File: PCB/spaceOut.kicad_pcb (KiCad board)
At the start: 2 copper layers, 98.5 x 59.9 mm, 9 parts, among them SW1 SW_Push, SW2 SW_Push, SW3 SW_Push, SW4 SW_Push, SW5 SW_Push, SW6 SW_Push, U1 MOUDLE-SEEEDUINO-XIAO

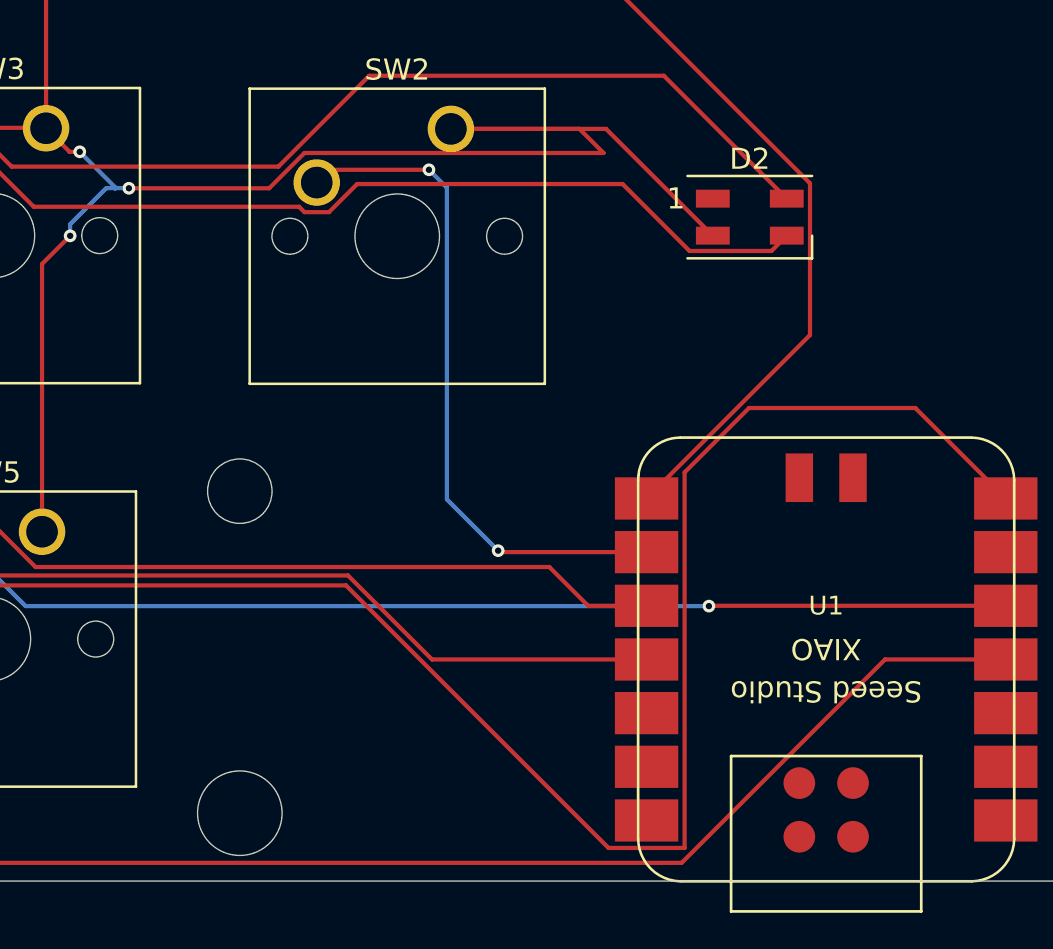
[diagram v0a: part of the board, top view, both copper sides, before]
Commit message: added global GND and 5V on XIAO
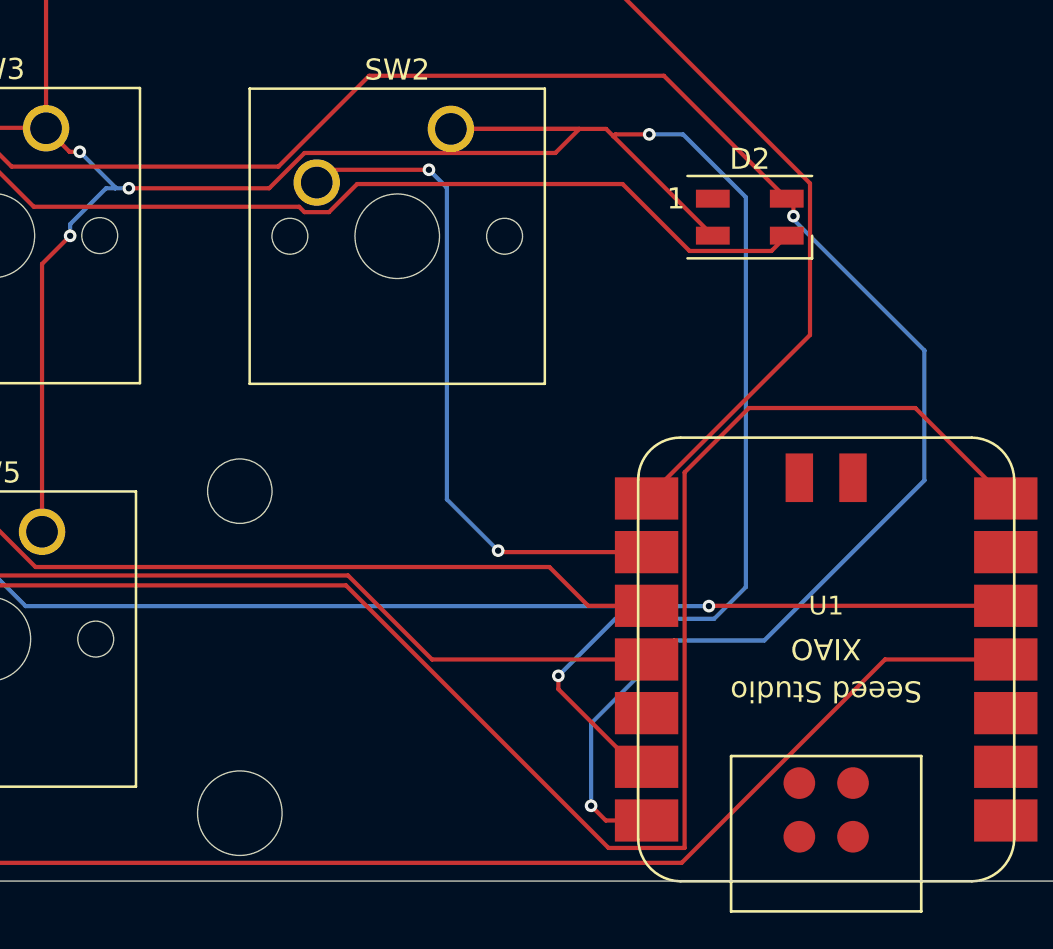
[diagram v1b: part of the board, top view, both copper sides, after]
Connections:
- U1 pad 13: unconnected-(U1-GND-Pad13) -> GND
- U1 pad 14: unconnected-(U1-5V-Pad14) -> +5V
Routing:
- net +5V: track 91.4 -> 134.8 mm, vias 0 -> 2
- net GND: track 146.1 -> 186.7 mm, vias 5 -> 7
